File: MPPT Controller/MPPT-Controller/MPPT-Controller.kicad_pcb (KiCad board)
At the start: 4 copper layers, 81 parts, among them J1 Conn_01x02_Pin, J2 Conn_01x02_Pin, J3 Conn_01x02_Pin, J4 Conn_01x02_Pin, J5 USB_C_Receptacle_USB2.0_16P, J6 Conn_01x02_Pin, M1 Fan_4pin, Q1 IRL540N, SW1 SW_SPDT, U1 ADS1115IDGS, U2 ESP32-WROOM-32D, U3 CH340C, U4 LM1117DT-3.3, U5 LM2596S-ADJ, U6 TC4422, U7 ADS1115IDGS

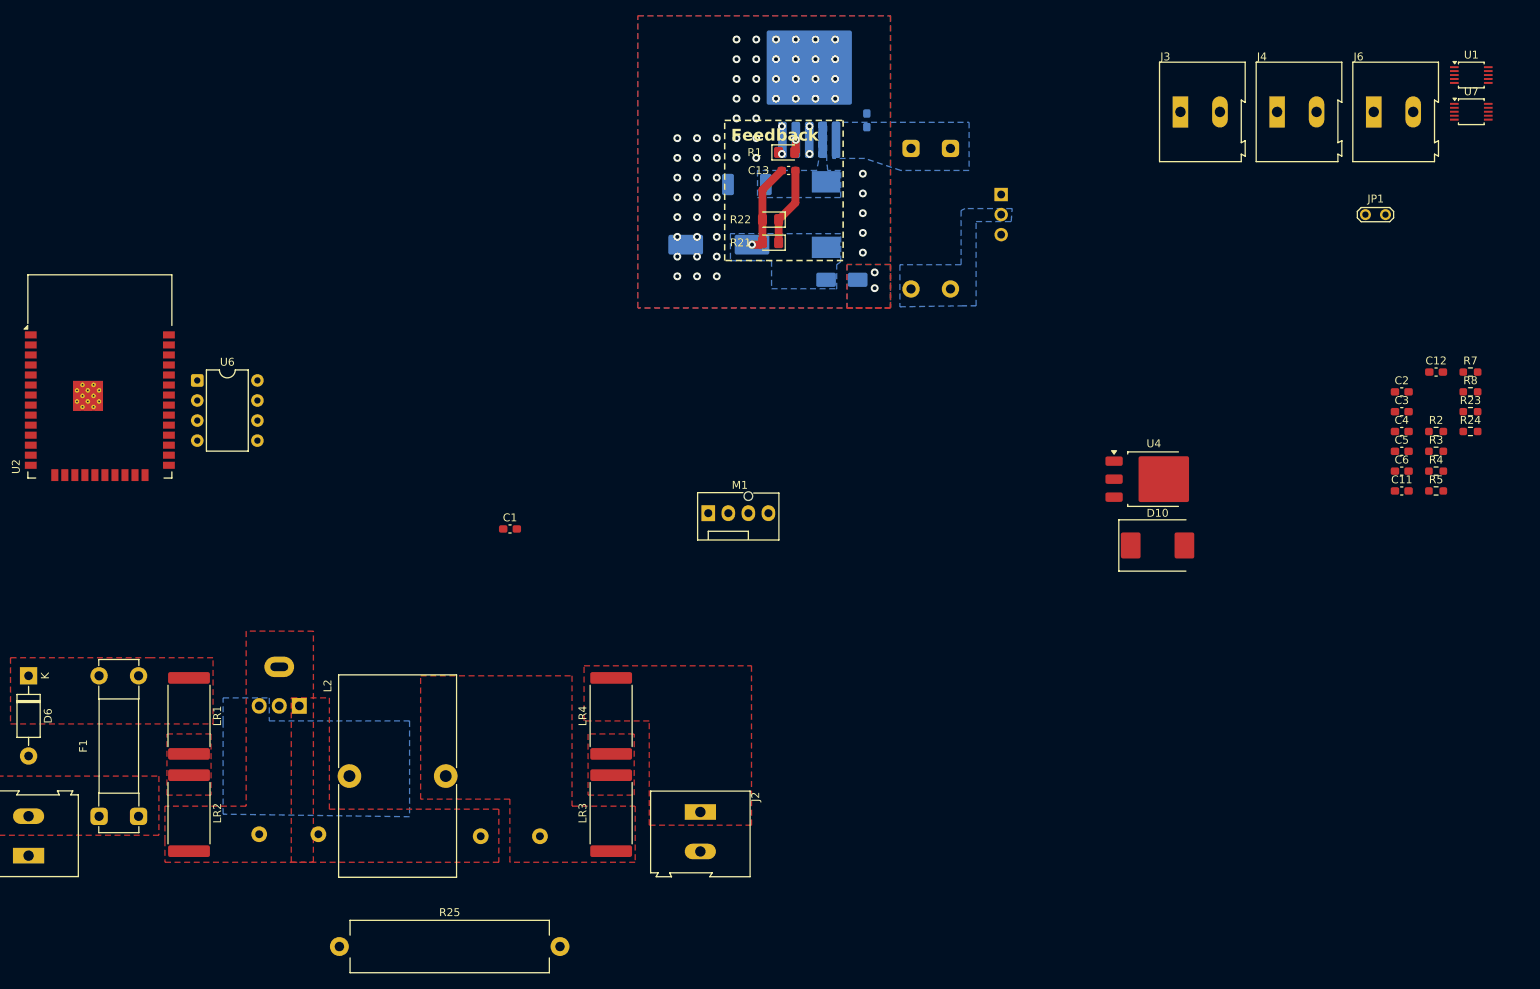
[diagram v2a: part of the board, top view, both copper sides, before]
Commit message: Add thermistor
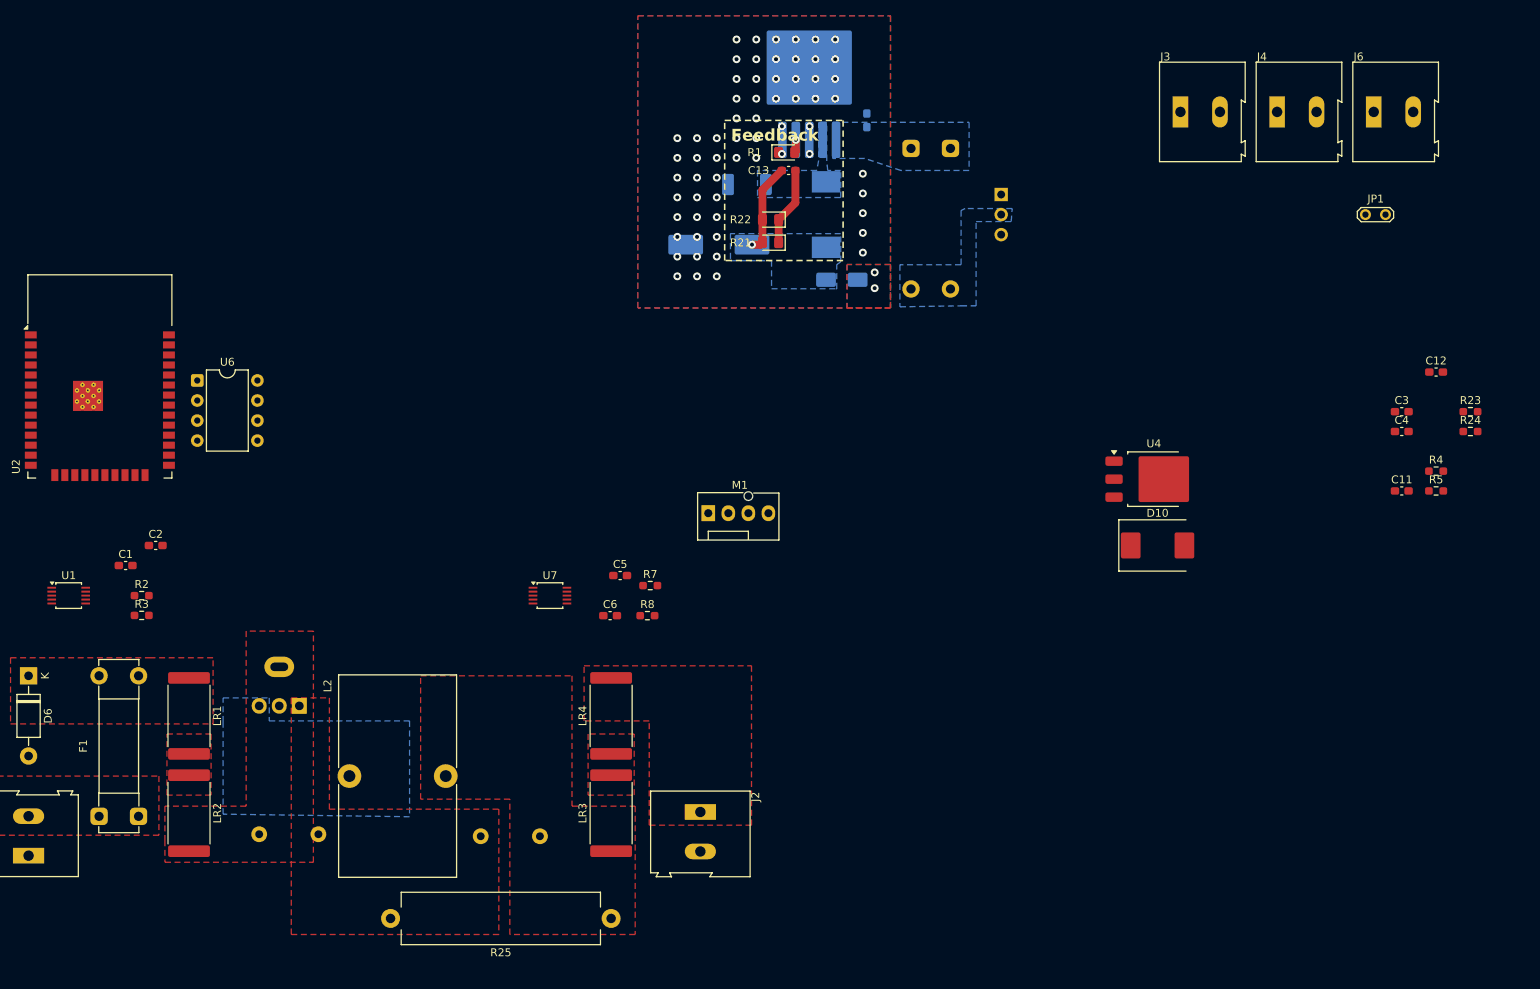
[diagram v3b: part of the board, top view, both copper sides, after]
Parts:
- moved U1 189.5 mm to (41.9, 91.4)
- moved R2 165.3 mm to (51.2, 91.4)
- moved R3 165.3 mm to (51.2, 94.0)
- moved C2 159.0 mm to (52.9, 85.1)
- moved U7 131.8 mm to (102.9, 91.4)
- moved R8 108.0 mm to (115.2, 94.0)
- moved R7 107.4 mm to (115.6, 90.2)
- moved C6 101.9 mm to (110.5, 94.0)
- moved C5 100.2 mm to (111.8, 88.9)
- moved C1 48.9 mm to (49.1, 87.6)
- moved R25 34.6 mm to (110.6, 132.3), turned to 180 degrees
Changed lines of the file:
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@@
 	(footprint "Capacitor_SMD:C_0603_1608Metric_Pad1.08x0.95mm_HandSolder"
 		(layer "F.Cu")
-		(at 210.76 75.675)
+		(at 110.49 93.98)
 		(descr "Capacitor SMD 0603 (1608 Metric), square (rectangular) end terminal, IPC-7351 nominal with elongated pad for handsoldering. (Body size source: IPC-SM-782 page 76, https://www.pcb-3d.com/wordpress/wp-content/uploads/ipc-sm-782a_amendment_1_and_2.pdf), generated with kicad-footprint-generator")
 		(tags "capacitor handsolder")
@@
 	(footprint "Package_SO:TSSOP-10_3x3mm_P0.5mm"
 		(layer "F.Cu")
-		(at 219.57 30.155)
+		(at 102.87 91.44)
 		(descr "TSSOP10: plastic thin shrink small outline package; 10 leads; body width 3 mm; (see NXP SSOP-TSSOP-VSO-REFLOW.pdf and sot552-1_po.pdf)")
 		(tags "SSOP 0.5")
@@
 	(footprint "Capacitor_SMD:C_0603_1608Metric_Pad1.08x0.95mm_HandSolder"
 		(layer "F.Cu")
-		(at 210.76 65.635)
+		(at 52.9325 85.09)
 		(descr "Capacitor SMD 0603 (1608 Metric), square (rectangular) end terminal, IPC-7351 nominal with elongated pad for handsoldering. (Body size source: IPC-SM-782 page 76, https://www.pcb-3d.com/wordpress/wp-content/uploads/ipc-sm-782a_amendment_1_and_2.pdf), generated with kicad-footprint-generator")
 		(tags "capacitor handsolder")
@@
 	(footprint "Resistor_SMD:R_0603_1608Metric_Pad0.98x0.95mm_HandSolder"
 		(layer "F.Cu")
-		(at 219.46 63.125)
+		(at 115.57 90.17)
 		(descr "Resistor SMD 0603 (1608 Metric), square (rectangular) end terminal, IPC-7351 nominal with elongated pad for handsoldering. (Body size source: IPC-SM-782 page 72, https://www.pcb-3d.com/wordpress/wp-content/uploads/ipc-sm-782a_amendment_1_and_2.pdf), generated with kicad-footprint-generator")
 		(tags "resistor handsolder")
@@
 	(footprint "Resistor_THT:R_Axial_Power_L25.0mm_W6.4mm_P27.94mm"
 		(layer "F.Cu")
-		(at 76.2 135.89)
+		(at 110.617 132.334 180)
 		(descr "Resistor, Axial_Power series, Box, pin pitch=27.94mm, 5W, length*width*height=25*6.4*6.4mm^3, http://cdn-reichelt.de/documents/datenblatt/B400/5WAXIAL_9WAXIAL_11WAXIAL_17WAXIAL%23YAG.pdf")
 		(tags "Resistor Axial_Power series Box pin pitch 27.94mm 5W length 25mm width 6.4mm height 6.4mm")
@@
 		)
 		(property "Datasheet" ""
-			(at 0 0 0)
+			(at 0 0 180)
 			(unlocked yes)
 			(layer "F.Fab")
@@
 		)
 		(property "Description" "Resistor"
-			(at 0 0 0)
+			(at 0 0 180)
 			(unlocked yes)
 			(layer "F.Fab")
@@
 		(attr through_hole)
 		(fp_line
-			(start 1.35 -3.32)
-			(end 26.59 -3.32)
+			(start 26.59 3.32)
+			(end 26.59 1.44)
 			(stroke
 				(width 0.12)
@@
 		)
 		(fp_line
-			(start 1.35 -1.44)
-			(end 1.35 -3.32)
+			(start 26.59 -3.32)
+			(end 26.59 -1.44)
 			(stroke
 				(width 0.12)
@@
 		)
 		(fp_line
-			(start 1.35 1.44)
-			(end 1.35 3.32)
+			(start 1.35 3.32)
+			(end 26.59 3.32)
 			(stroke
 				(width 0.12)
@@
 		)
 		(fp_line
-			(start 1.35 3.32)
-			(end 26.59 3.32)
+			(start 1.35 1.44)
+			(end 1.35 3.32)
 			(stroke
 				(width 0.12)
@@
 		)
 		(fp_line
-			(start 26.59 -3.32)
-			(end 26.59 -1.44)
+			(start 1.35 -1.44)
+			(end 1.35 -3.32)
 			(stroke
 				(width 0.12)
@@
 		)
 		(fp_line
-			(start 26.59 3.32)
-			(end 26.59 1.44)
+			(start 1.35 -3.32)
+			(end 26.59 -3.32)
 			(stroke
 				(width 0.12)
@@
 		)
 		(fp_line
-			(start -1.45 -3.45)
-			(end -1.45 3.45)
+			(start 29.39 3.45)
+			(end 29.39 -3.45)
 			(stroke
 				(width 0.05)
@@
 		)
 		(fp_line
-			(start -1.45 3.45)
-			(end 29.39 3.45)
+			(start 29.39 -3.45)
+			(end -1.45 -3.45)
 			(stroke
 				(width 0.05)
@@
 		)
 		(fp_line
-			(start 29.39 -3.45)
-			(end -1.45 -3.45)
+			(start -1.45 3.45)
+			(end 29.39 3.45)
 			(stroke
 				(width 0.05)
@@
 		)
 		(fp_line
-			(start 29.39 3.45)
-			(end 29.39 -3.45)
+			(start -1.45 -3.45)
+			(end -1.45 3.45)
 			(stroke
 				(width 0.05)
@@
 		)
 		(fp_line
-			(start 0 0)
-			(end 1.47 0)
+			(start 27.94 0)
+			(end 26.47 0)
 			(stroke
 				(width 0.1)
@@
 		)
 		(fp_line
-			(start 1.47 -3.2)
-			(end 1.47 3.2)
+			(start 26.47 3.2)
+			(end 26.47 -3.2)
 			(stroke
 				(width 0.1)
@@
 		)
 		(fp_line
-			(start 1.47 3.2)
-			(end 26.47 3.2)
+			(start 26.47 -3.2)
+			(end 1.47 -3.2)
 			(stroke
 				(width 0.1)
@@
 		)
 		(fp_line
-			(start 26.47 -3.2)
-			(end 1.47 -3.2)
+			(start 1.47 3.2)
+			(end 26.47 3.2)
 			(stroke
 				(width 0.1)
@@
 		)
 		(fp_line
-			(start 26.47 3.2)
-			(end 26.47 -3.2)
+			(start 1.47 -3.2)
+			(end 1.47 3.2)
 			(stroke
 				(width 0.1)
@@
 		)
 		(fp_line
-			(start 27.94 0)
-			(end 26.47 0)
+			(start 0 0)
+			(end 1.47 0)
 			(stroke
 				(width 0.1)
@@
 		)
 		(pad "1" thru_hole circle
-			(at 0 0)
+			(at 0 0 180)
 			(size 2.4 2.4)
 			(drill 1.2)
@@
 		)
 		(pad "2" thru_hole oval
-			(at 27.94 0)
+			(at 27.94 0 180)
 			(size 2.4 2.4)
 			(drill 1.2)
@@
 	(footprint "Capacitor_SMD:C_0603_1608Metric_Pad1.08x0.95mm_HandSolder"
 		(layer "F.Cu")
-		(at 97.81 83)
+		(at 49.1225 87.63)
 		(descr "Capacitor SMD 0603 (1608 Metric), square (rectangular) end terminal, IPC-7351 nominal with elongated pad for handsoldering. (Body size source: IPC-SM-782 page 76, https://www.pcb-3d.com/wordpress/wp-content/uploads/ipc-sm-782a_amendment_1_and_2.pdf), generated with kicad-footprint-generator")
 		(tags "capacitor handsolder")
@@
 	(footprint "Resistor_SMD:R_0603_1608Metric_Pad0.98x0.95mm_HandSolder"
 		(layer "F.Cu")
-		(at 215.11 73.165)
+		(at 51.1575 93.95)
 		(descr "Resistor SMD 0603 (1608 Metric), square (rectangular) end terminal, IPC-7351 nominal with elongated pad for handsoldering. (Body size source: IPC-SM-782 page 72, https://www.pcb-3d.com/wordpress/wp-content/uploads/ipc-sm-782a_amendment_1_and_2.pdf), generated with kicad-footprint-generator")
 		(tags "resistor handsolder")
@@
 	(footprint "Resistor_SMD:R_0603_1608Metric_Pad0.98x0.95mm_HandSolder"
 		(layer "F.Cu")
-		(at 215.11 70.655)
+		(at 51.1575 91.44)
 		(descr "Resistor SMD 0603 (1608 Metric), square (rectangular) end terminal, IPC-7351 nominal with elongated pad for handsoldering. (Body size source: IPC-SM-782 page 72, https://www.pcb-3d.com/wordpress/wp-content/uploads/ipc-sm-782a_amendment_1_and_2.pdf), generated with kicad-footprint-generator")
 		(tags "resistor handsolder")
@@
 	(footprint "Package_SO:TSSOP-10_3x3mm_P0.5mm"
 		(layer "F.Cu")
-		(at 219.57 25.505)
+		(at 41.91 91.44)
 		(descr "TSSOP10: plastic thin shrink small outline package; 10 leads; body width 3 mm; (see NXP SSOP-TSSOP-VSO-REFLOW.pdf and sot552-1_po.pdf)")
 		(tags "SSOP 0.5")
@@
 	(footprint "Capacitor_SMD:C_0603_1608Metric_Pad1.08x0.95mm_HandSolder"
 		(layer "F.Cu")
-		(at 210.76 73.165)
+		(at 111.76 88.9)
 		(descr "Capacitor SMD 0603 (1608 Metric), square (rectangular) end terminal, IPC-7351 nominal with elongated pad for handsoldering. (Body size source: IPC-SM-782 page 76, https://www.pcb-3d.com/wordpress/wp-content/uploads/ipc-sm-782a_amendment_1_and_2.pdf), generated with kicad-footprint-generator")
 		(tags "capacitor handsolder")
@@
 	(footprint "Resistor_SMD:R_0603_1608Metric_Pad0.98x0.95mm_HandSolder"
 		(layer "F.Cu")
-		(at 219.46 65.635)
+		(at 115.2125 93.98)
 		(descr "Resistor SMD 0603 (1608 Metric), square (rectangular) end terminal, IPC-7351 nominal with elongated pad for handsoldering. (Body size source: IPC-SM-782 page 72, https://www.pcb-3d.com/wordpress/wp-content/uploads/ipc-sm-782a_amendment_1_and_2.pdf), generated with kicad-footprint-generator")
 		(tags "resistor handsolder")
@@
 		(polygon
 			(pts
-				(xy 97.79 125.222) (xy 97.79 117.221) (xy 86.487 117.221) (xy 86.487 101.6) (xy 105.664 101.6) (xy 105.664 118.11)
-				(xy 113.665 118.11) (xy 113.665 125.222)
+				(xy 97.79 134.366) (xy 97.79 117.221) (xy 86.487 117.221) (xy 86.487 101.6) (xy 105.664 101.6) (xy 105.664 118.11)
+				(xy 113.665 118.11) (xy 113.665 134.366)
 			)
 		)
@@
 		(polygon
 			(pts
-				(xy 70.104 104.394) (xy 74.93 104.394) (xy 74.93 118.491) (xy 96.393 118.491) (xy 96.393 125.222)
-				(xy 70.104 125.222) (xy 70.104 104.394)
+				(xy 70.104 104.394) (xy 74.93 104.394) (xy 74.93 118.491) (xy 96.393 118.491) (xy 96.393 134.366)
+				(xy 70.104 134.366) (xy 70.104 104.394)
 			)
 		)

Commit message: Diode
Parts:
- added J7: Conn_01x02_Pin, Connector_PinHeader_2.54mm:PinHeader_1x02_P2.54mm_Vertical, F.Cu at (93.3, 35.1)
- added J8: Conn_01x02_Pin, Connector_PinHeader_2.54mm:PinHeader_1x02_P2.54mm_Vertical, F.Cu at (97.9, 35.1)
- added R26: 10k, LED_SMD:LED_0805_2012Metric_Pad1.15x1.40mm_HandSolder, F.Cu at (88.6, 34.4)
- added R27: 10k, LED_SMD:LED_0805_2012Metric_Pad1.15x1.40mm_HandSolder, F.Cu at (88.6, 37.4)
- added R28: 10k, LED_SMD:LED_0805_2012Metric_Pad1.15x1.40mm_HandSolder, F.Cu at (88.6, 40.4)
- added R29: 10k, LED_SMD:LED_0805_2012Metric_Pad1.15x1.40mm_HandSolder, F.Cu at (88.6, 43.5)
- added TH1: NTC, Resistor_THT:R_Axial_DIN0204_L3.6mm_D1.6mm_P1.90mm_Vertical, F.Cu at (92.7, 42.7)
- added TH2: NTC, Resistor_THT:R_Axial_DIN0204_L3.6mm_D1.6mm_P1.90mm_Vertical, F.Cu at (92.7, 45.8)
- D10: moved to B.Cu
- moved D10 102.2 mm to (83.1, 117.9), turned to -90 degrees
- moved C2 13.7 mm to (59.7, 97.0), turned to 90 degrees
- moved U1 13.6 mm to (55.4, 89.7), turned to 90 degrees
- moved C1 10.1 mm to (52.8, 97.0), turned to 90 degrees
- moved R3 7.42 mm to (57.9, 97.0), turned to 90 degrees
- moved R2 6.57 mm to (54.6, 97.0), turned to 90 degrees
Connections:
- U1 pad 2: unconnected-(U1-ALERT/RDY-Pad2) -> RDY1
- U1 pad 7: unconnected-(U1-AIN3-Pad7) -> Aux1
- U2 pad 30: unconnected-(U2-IO18-Pad30) -> RDY1
- U2 pad 31: unconnected-(U2-IO19-Pad31) -> RDY2
- U2 pad 6: unconnected-(U2-IO34-Pad6) -> HeatsinkT
- U2 pad 9: unconnected-(U2-IO33-Pad9) -> AmbientT
- U7 pad 2: unconnected-(U7-ALERT/RDY-Pad2) -> RDY2
- U7 pad 7: unconnected-(U7-AIN3-Pad7) -> Aux2
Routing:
- net IdiffB: track 0.00 -> 5.05 mm
- net IdiffA: track 0.00 -> 4.83 mm
- net Net-(D10-A): vias 0 -> 11
- added copper zone on B.Cu, net Net-(D10-A)

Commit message: Update MPPT-Controller.kicad_pcb
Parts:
- moved R23 132.5 mm to (87.3, 77.2)
- moved R24 132.5 mm to (87.3, 79.8)
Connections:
- Q1 pad 1: Net-(D10-A) -> Net-(Q1-G)
- R23 pad 2: Net-(D10-A) -> Net-(Q1-G)
- R24 pad 2: Net-(D10-A) -> Net-(Q1-G)
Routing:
- added copper zone on In1.Cu, net Net-(D10-A)
- added copper zone on In2.Cu, net Net-(D10-A)
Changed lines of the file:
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@@
 	(net 89 "RDY1")
 	(net 90 "RDY2")
+	(net 91 "Net-(Q1-G)")
 	(footprint "Resistor_THT:R_Axial_DIN0204_L3.6mm_D1.6mm_P1.90mm_Vertical"
 		(layer "F.Cu")
@@
 	(footprint "Resistor_SMD:R_0603_1608Metric_Pad0.98x0.95mm_HandSolder"
 		(layer "F.Cu")
-		(at 219.46 70.655)
+		(at 87.2725 79.756)
 		(descr "Resistor SMD 0603 (1608 Metric), square (rectangular) end terminal, IPC-7351 nominal with elongated pad for handsoldering. (Body size source: IPC-SM-782 page 72, https://www.pcb-3d.com/wordpress/wp-content/uploads/ipc-sm-782a_amendment_1_and_2.pdf), generated with kicad-footprint-generator")
 		(tags "resistor handsolder")
@@
 			(layers "F.Cu" "F.Mask" "F.Paste")
 			(roundrect_rratio 0.25)
-			(net 15 "Net-(D10-A)")
+			(net 91 "Net-(Q1-G)")
 			(pintype "passive")
 		)
@@
 	(footprint "Resistor_SMD:R_0603_1608Metric_Pad0.98x0.95mm_HandSolder"
 		(layer "F.Cu")
-		(at 219.46 68.145)
+		(at 87.2725 77.246)
 		(descr "Resistor SMD 0603 (1608 Metric), square (rectangular) end terminal, IPC-7351 nominal with elongated pad for handsoldering. (Body size source: IPC-SM-782 page 72, https://www.pcb-3d.com/wordpress/wp-content/uploads/ipc-sm-782a_amendment_1_and_2.pdf), generated with kicad-footprint-generator")
 		(tags "resistor handsolder")
@@
 			(layers "F.Cu" "F.Mask" "F.Paste")
 			(roundrect_rratio 0.25)
-			(net 15 "Net-(D10-A)")
+			(net 91 "Net-(Q1-G)")
 			(pintype "passive")
 		)
@@
 			(layers "*.Cu" "*.Mask")
 			(remove_unused_layers no)
-			(net 15 "Net-(D10-A)")
+			(net 91 "Net-(Q1-G)")
 			(pinfunction "G")
 			(pintype "input")
@@
 		(polygon
 			(pts
-				(xy 70.104 104.394) (xy 74.93 104.394) (xy 74.93 118.491) (xy 96.393 118.491) (xy 96.393 134.366)
+				(xy 70.104 118.364) (xy 74.93 118.364) (xy 74.93 118.364) (xy 96.393 118.364) (xy 96.393 134.366)
 				(xy 70.104 134.366)
 			)
@@
 		(layers "F.Cu" "B.Cu" "In1.Cu" "In2.Cu")
 		(hatch edge 0.5)
-		(priority 6)
-		(connect_pads thru_hole_only
-			(clearance 0.75)
-		)
-		(min_thickness 0.25)
-		(filled_areas_thickness no)
-		(fill
-			(thermal_gap 0.5)
-			(thermal_bridge_width 0.5)
-		)
-		(polygon
-			(pts
-				(xy 27.686303 98.939053) (xy 27.686303 135.508046) (xy 129.032303 135.762046) (xy 129.032303 98.939053)
-			)
-		)
-	)
-	(zone
-		(net 2)
-		(net_name "GND")
-		(layers "F.Cu" "B.Cu" "In1.Cu" "In2.Cu")
-		(hatch edge 0.5)
 		(priority 2)
 		(connect_pads thru_hole_only
@@
 	)
 	(zone
-		(net 0)
-		(net_name "")
-		(layer "F.Mask")
-		(hatch edge 0.5)
-		(priority 7)
-		(connect_pads yes
-			(clearance 0.6)
-		)
-		(min_thickness 0.25)
-		(filled_areas_thickness no)
-		(fill yes
-			(thermal_gap 0)
-			(thermal_bridge_width 1)
-		)
-		(polygon
-			(pts
-				(xy 64.389 120.142) (xy 64.389 125.222) (xy 69.342 125.222) (xy 69.342 107.315) (xy 64.389 107.315)
-			)
-		)
-	)
-	(zone
-		(net 0)
-		(net_name "")
-		(layer "F.Mask")
-		(hatch edge 0.5)
-		(priority 8)
-		(connect_pads yes
-			(clearance 0.5)
-		)
-		(min_thickness 0.25)
-		(filled_areas_thickness no)
-		(fill yes
-			(thermal_gap 0)
-			(thermal_bridge_width 1)
-		)
-		(polygon
-			(pts
-				(xy 70.1 107.321) (xy 74.93 107.321) (xy 74.93 118.493) (xy 74.93 125.224) (xy 70.1 125.224)
-			)
-		)
-	)
-	(zone
 		(net 13)
 		(net_name "Net-(D8-A)")
@@
 		(polygon
 			(pts
-				(xy 61.468 104.394) (xy 67.31 104.394) (xy 67.31 107.315) (xy 85.09 107.315) (xy 85.09 119.449589)
-				(xy 61.468 119.126) (xy 61.468 107.442)
+				(xy 63.5 104.394) (xy 67.31 104.394) (xy 67.31 108.331) (xy 85.09 108.331) (xy 85.09 117.094) (xy 63.5 117.094)
+				(xy 63.5 107.696)
 			)
 		)
@@
 		(net 15)
 		(net_name "Net-(D10-A)")
-		(layer "B.Cu")
+		(layers "B.Cu" "In1.Cu" "In2.Cu")
 		(hatch edge 0.5)
 		(priority 16)
